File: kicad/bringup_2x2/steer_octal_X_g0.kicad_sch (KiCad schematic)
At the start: 42 parts

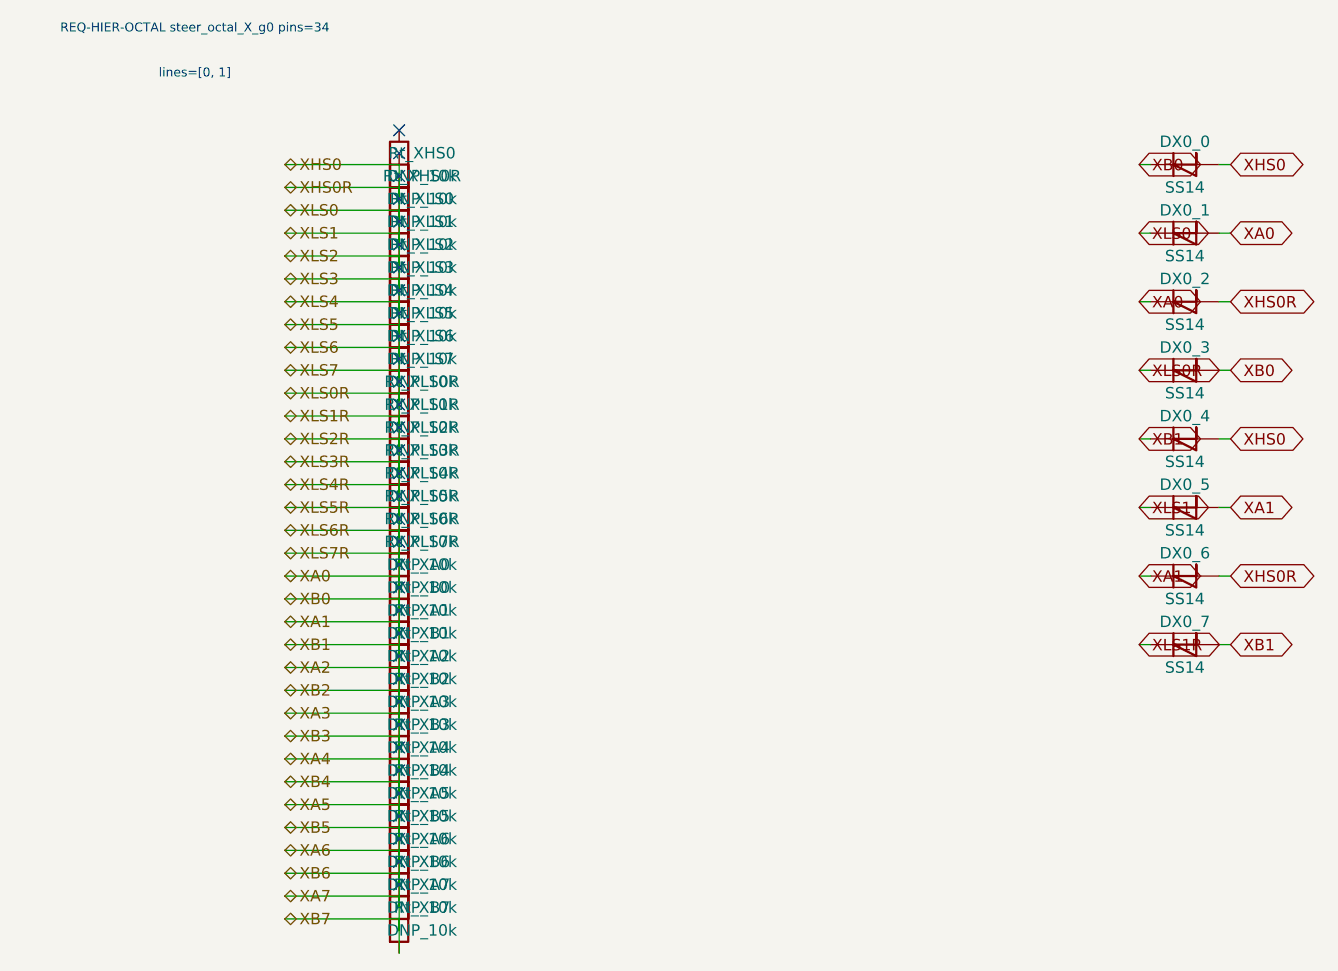
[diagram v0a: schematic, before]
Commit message: logical seperation into host and multiple decode/drive/steering boards
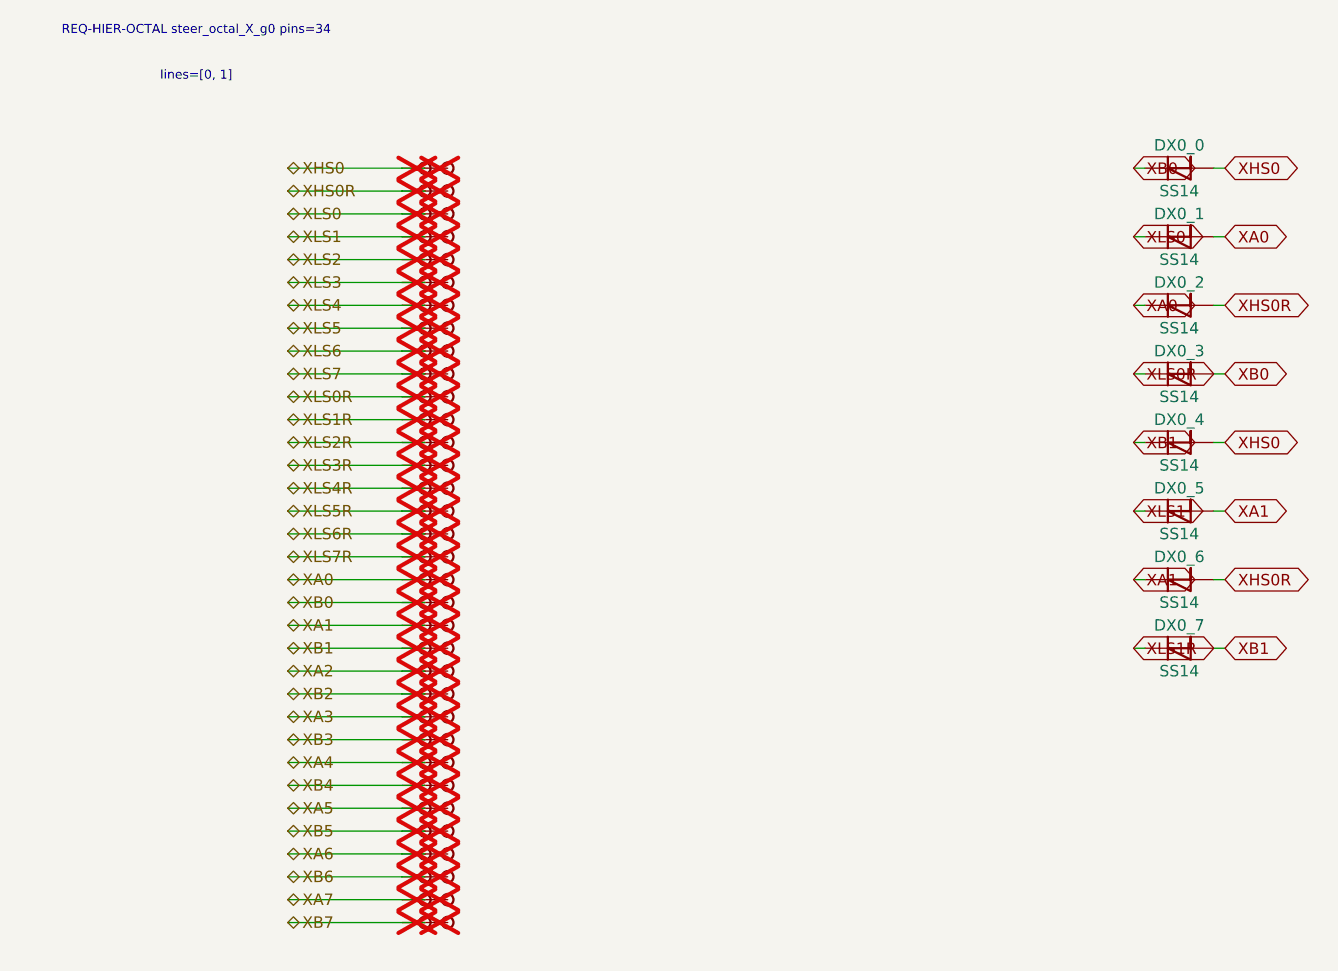
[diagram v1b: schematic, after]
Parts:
- removed Rt_XA0, Rt_XA1, Rt_XA2, Rt_XA3, Rt_XA4, Rt_XA5, Rt_XA6, Rt_XA7, Rt_XB0, Rt_XB1, Rt_XB2, Rt_XB3, Rt_XB4, Rt_XB5, Rt_XB6, Rt_XB7, Rt_XHS0, Rt_XHS0R, Rt_XLS0, Rt_XLS0R, Rt_XLS1, Rt_XLS1R, Rt_XLS2, Rt_XLS2R, Rt_XLS3, Rt_XLS3R, Rt_XLS4, Rt_XLS4R, Rt_XLS5, Rt_XLS5R, Rt_XLS6, Rt_XLS6R, Rt_XLS7, Rt_XLS7R: DNP_10k, symbol Device:R
- added TP_XA0, TP_XA0b, TP_XA1, TP_XA1b, TP_XA2, TP_XA2b, TP_XA3, TP_XA3b, TP_XA4, TP_XA4b, TP_XA5, TP_XA5b, TP_XA6, TP_XA6b, TP_XA7, TP_XA7b, TP_XB0, TP_XB0b, TP_XB1, TP_XB1b, TP_XB2, TP_XB2b, TP_XB3, TP_XB3b, TP_XB4, TP_XB4b, TP_XB5, TP_XB5b, TP_XB6, TP_XB6b, TP_XB7, TP_XB7b, TP_XHS0, TP_XHS0R, TP_XHS0Rb, TP_XHS0b, TP_XLS0, TP_XLS0R, TP_XLS0Rb, TP_XLS0b, TP_XLS1, TP_XLS1R, TP_XLS1Rb, TP_XLS1b, TP_XLS2, TP_XLS2R, TP_XLS2Rb, TP_XLS2b, TP_XLS3, TP_XLS3R, TP_XLS3Rb, TP_XLS3b, TP_XLS4, TP_XLS4R, TP_XLS4Rb, TP_XLS4b, TP_XLS5, TP_XLS5R, TP_XLS5Rb, TP_XLS5b, TP_XLS6, TP_XLS6R, TP_XLS6Rb, TP_XLS6b, TP_XLS7, TP_XLS7R, TP_XLS7Rb, TP_XLS7b: Stub, symbol CMR:Stub
- DX0_0, DX0_1, DX0_2, DX0_3, DX0_4, DX0_5, DX0_6, DX0_7: symbol Device:D_Schottky -> CMR:D_Schottky
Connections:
- net XA0: now also TP_XA0.1, TP_XA0b.1; no longer DX0_0.1 (K), DX0_0.2 (A), DX0_1.1 (K), DX0_2.2 (A), DX0_3.1 (K), DX0_3.2 (A), DX0_4.1 (K), DX0_4.2 (A), DX0_5.1 (K), DX0_5.2 (A), DX0_6.1 (K), DX0_6.2 (A), DX0_7.1 (K), DX0_7.2 (A)
- new net XA1: DX0_5.2 (A), DX0_6.1 (K), TP_XA1.1, TP_XA1b.1
- new net XA2: TP_XA2.1, TP_XA2b.1
- new net XA3: TP_XA3.1, TP_XA3b.1
- new net XA4: TP_XA4.1, TP_XA4b.1
- new net XA5: TP_XA5.1, TP_XA5b.1
- new net XA6: TP_XA6.1, TP_XA6b.1
- new net XA7: TP_XA7.1, TP_XA7b.1
- new net XB0: DX0_0.1 (K), DX0_3.2 (A), TP_XB0.1, TP_XB0b.1
- new net XB1: DX0_4.1 (K), DX0_7.2 (A), TP_XB1.1, TP_XB1b.1
- new net XB2: TP_XB2.1, TP_XB2b.1
- new net XB3: TP_XB3.1, TP_XB3b.1
- new net XB4: TP_XB4.1, TP_XB4b.1
- new net XB5: TP_XB5.1, TP_XB5b.1
- new net XB6: TP_XB6.1, TP_XB6b.1
- new net XB7: TP_XB7.1, TP_XB7b.1
- new net XHS0: DX0_0.2 (A), DX0_4.2 (A), TP_XHS0.1, TP_XHS0b.1
- new net XHS0R: DX0_2.2 (A), DX0_6.2 (A), TP_XHS0R.1, TP_XHS0Rb.1
- new net XLS0: DX0_1.1 (K), TP_XLS0.1, TP_XLS0b.1
- new net XLS0R: DX0_3.1 (K), TP_XLS0R.1, TP_XLS0Rb.1
- new net XLS1: DX0_5.1 (K), TP_XLS1.1, TP_XLS1b.1
- new net XLS1R: DX0_7.1 (K), TP_XLS1R.1, TP_XLS1Rb.1
- new net XLS2: TP_XLS2.1, TP_XLS2b.1
- new net XLS2R: TP_XLS2R.1, TP_XLS2Rb.1
- new net XLS3: TP_XLS3.1, TP_XLS3b.1
- new net XLS3R: TP_XLS3R.1, TP_XLS3Rb.1
- new net XLS4: TP_XLS4.1, TP_XLS4b.1
- new net XLS4R: TP_XLS4R.1, TP_XLS4Rb.1
- new net XLS5: TP_XLS5.1, TP_XLS5b.1
- new net XLS5R: TP_XLS5R.1, TP_XLS5Rb.1
- new net XLS6: TP_XLS6.1, TP_XLS6b.1
- new net XLS6R: TP_XLS6R.1, TP_XLS6Rb.1
- new net XLS7: TP_XLS7.1, TP_XLS7b.1
- new net XLS7R: TP_XLS7R.1, TP_XLS7Rb.1
- no-connect marks 34 -> 0
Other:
- moved on the sheet: DX0_0, DX0_1, DX0_2, DX0_3, DX0_4, DX0_5, DX0_6, DX0_7
